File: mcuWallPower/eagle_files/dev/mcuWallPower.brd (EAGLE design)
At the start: 30 x 30 mm, 3 parts, among them P1 CR2032

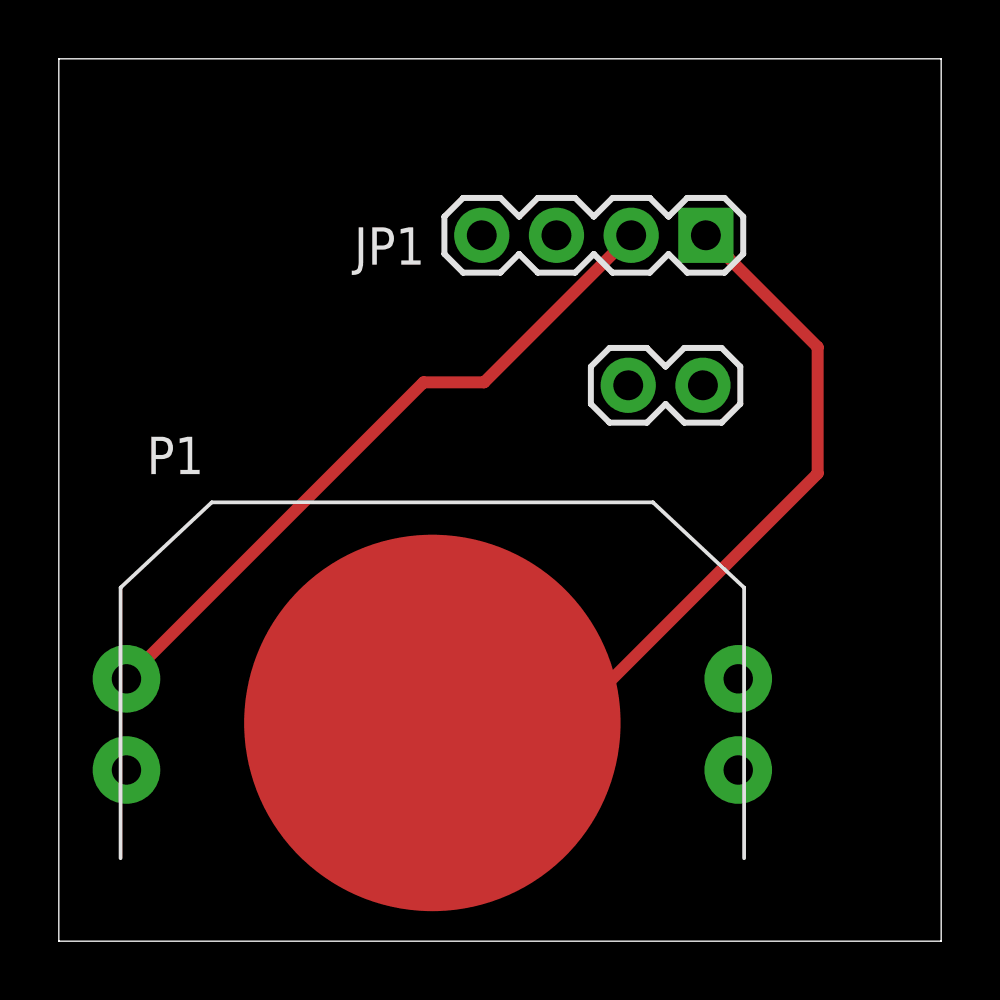
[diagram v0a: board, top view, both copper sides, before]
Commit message: Added USB mini connector to board along with other components. Todo: Replace USB mini connector with USB micro B connector. Looks like I'll need to make a custom footprint.
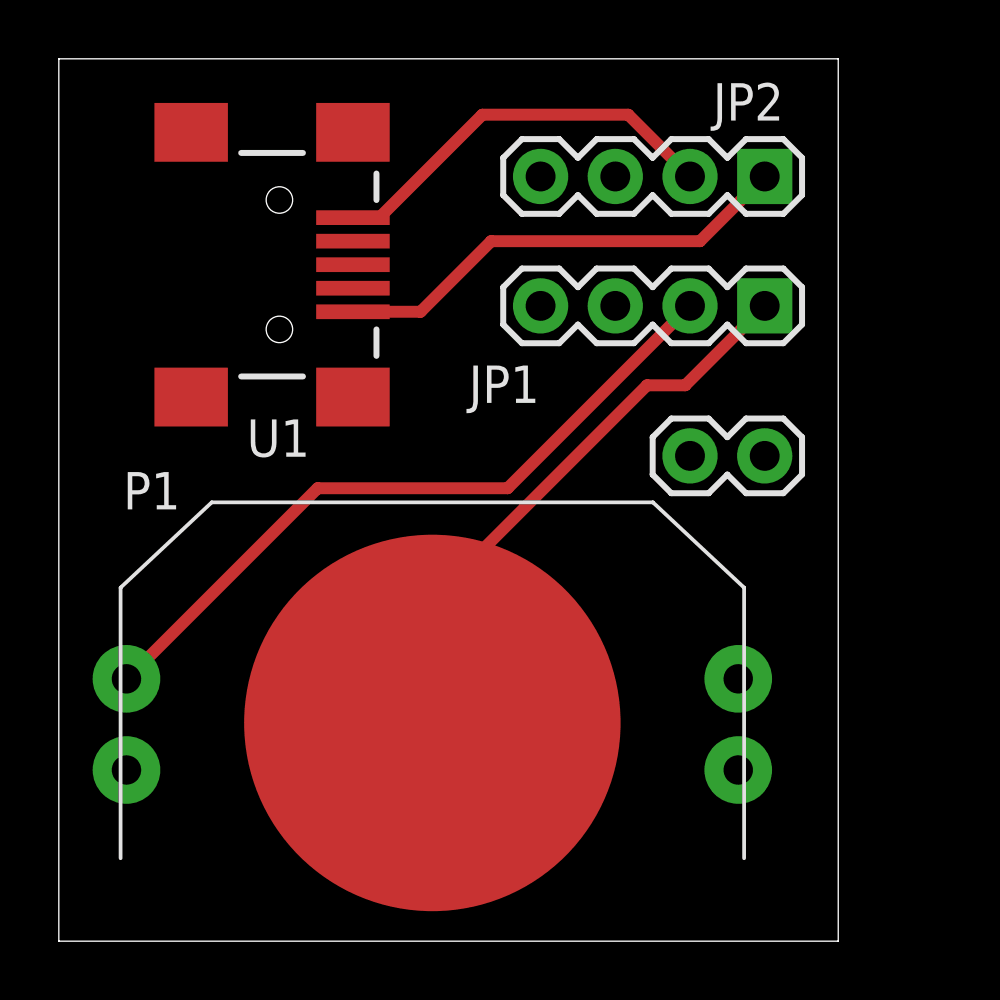
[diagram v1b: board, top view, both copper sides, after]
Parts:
- added JP2: (no value), SparkFun-Connectors:1X04
- added U1: USB-MINIB-5PIN, SparkFun-Connectors:USB-MINIB
- moved JP3 3.19 mm to (24.0, 16.5)
- moved JP1 3.12 mm to (24.0, 21.6)
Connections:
- new net N$3: JP2.1, U1.GND
- new net N$4: JP2.2, U1.VBUS
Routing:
- net N$3: track 0.00 -> 15.9 mm
- net N$4: track 0.00 -> 13.8 mm
- net N$2: track 26.3 -> 19.6 mm
- net N$1: track 23.4 -> 24.4 mm
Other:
- board size 30 x 30 mm -> 26.5 x 30 mm
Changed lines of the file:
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@@
 <board>
 <plain>
-<wire x1="0" y1="0" x2="30" y2="0" width="0" layer="20"/>
-<wire x1="30" y1="0" x2="30" y2="30" width="0" layer="20"/>
-<wire x1="30" y1="30" x2="0" y2="30" width="0" layer="20"/>
+<wire x1="0" y1="0" x2="26.5" y2="0" width="0" layer="20"/>
+<wire x1="26.5" y1="0" x2="26.5" y2="30" width="0" layer="20"/>
+<wire x1="26.5" y1="30" x2="0" y2="30" width="0" layer="20"/>
 <wire x1="0" y1="30" x2="0" y2="0" width="0" layer="20"/>
 </plain>
@@
 <elements>
 <element name="P1" library="freddyLibr" package="CR2032/2025" value="CR2032" x="12.7" y="7.42" smashed="yes">
-<attribute name="NAME" x="2.99" y="15.88" size="1.27" layer="25"/>
-</element>
-<element name="JP1" library="SparkFun-Connectors" package="1X04" value="" x="22" y="24" smashed="yes" rot="R180">
-<attribute name="NAME" x="12.4462" y="24.2712" size="1.27" layer="25" ratio="10" rot="R180"/>
-<attribute name="VALUE" x="23.27" y="27.175" size="1.27" layer="27" rot="R180"/>
-</element>
-<element name="JP3" library="SparkFun-Connectors" package="1X02" value="M02PTH" x="21.9" y="18.9" smashed="yes" rot="R180"/>
+<attribute name="NAME" x="2.19" y="14.68" size="1.27" layer="25"/>
+</element>
+<element name="JP1" library="SparkFun-Connectors" package="1X04" value="" x="24" y="21.6" smashed="yes" rot="R180">
+<attribute name="NAME" x="16.3462" y="19.5712" size="1.27" layer="25" ratio="10" rot="R180"/>
+<attribute name="VALUE" x="25.27" y="24.775" size="1.27" layer="27" rot="R180"/>
+</element>
+<element name="JP3" library="SparkFun-Connectors" package="1X02" value="M02PTH" x="24" y="16.5" smashed="yes" rot="R180"/>
+<element name="U1" library="SparkFun-Connectors" package="USB-MINIB" value="USB-MINIB-5PIN" x="7.5" y="23" smashed="yes">
+<attribute name="NAME" x="6.39" y="16.47" size="1.27" layer="25"/>
+</element>
+<element name="JP2" library="SparkFun-Connectors" package="1X04" value="" x="24" y="26" smashed="yes" rot="R180">
+<attribute name="NAME" x="24.6462" y="29.1712" size="1.27" layer="25" ratio="10" rot="R180"/>
+<attribute name="VALUE" x="25.27" y="29.175" size="1.27" layer="27" rot="R180"/>
+</element>
 </elements>
 <signals>
@@
 <contactref element="JP1" pad="2"/>
 <wire x1="2.3" y1="8.92" x2="2.32" y2="8.92" width="0.4064" layer="1"/>
-<wire x1="2.32" y1="8.92" x2="12.4" y2="19" width="0.4064" layer="1"/>
-<wire x1="12.4" y1="19" x2="14.46" y2="19" width="0.4064" layer="1"/>
-<wire x1="14.46" y1="19" x2="19.46" y2="24" width="0.4064" layer="1"/>
+<wire x1="2.32" y1="8.92" x2="8.8" y2="15.4" width="0.4064" layer="1"/>
+<wire x1="8.8" y1="15.4" x2="15.26" y2="15.4" width="0.4064" layer="1"/>
+<wire x1="15.26" y1="15.4" x2="21.46" y2="21.6" width="0.4064" layer="1"/>
 </signal>
 <signal name="N$2">
 <contactref element="P1" pad="GND"/>
 <contactref element="JP1" pad="1"/>
-<wire x1="12.7" y1="7.42" x2="17.32" y2="7.42" width="0.4064" layer="1"/>
-<wire x1="17.32" y1="7.42" x2="25.8" y2="15.9" width="0.4064" layer="1"/>
-<wire x1="25.8" y1="15.9" x2="25.8" y2="20.2" width="0.4064" layer="1"/>
-<wire x1="25.8" y1="20.2" x2="22" y2="24" width="0.4064" layer="1"/>
+<wire x1="12.7" y1="7.42" x2="12.7" y2="11.6" width="0.4064" layer="1"/>
+<wire x1="12.7" y1="11.6" x2="20" y2="18.9" width="0.4064" layer="1"/>
+<wire x1="20" y1="18.9" x2="21.3" y2="18.9" width="0.4064" layer="1"/>
+<wire x1="21.3" y1="18.9" x2="24" y2="21.6" width="0.4064" layer="1"/>
+</signal>
+<signal name="N$3">
+<contactref element="U1" pad="GND"/>
+<contactref element="JP2" pad="1"/>
+<wire x1="10" y1="21.4" x2="12.3" y2="21.4" width="0.4064" layer="1"/>
+<wire x1="12.3" y1="21.4" x2="14.7" y2="23.8" width="0.4064" layer="1"/>
+<wire x1="14.7" y1="23.8" x2="21.8" y2="23.8" width="0.4064" layer="1"/>
+<wire x1="21.8" y1="23.8" x2="24" y2="26" width="0.4064" layer="1"/>
+</signal>
+<signal name="N$4">
+<contactref element="U1" pad="VBUS"/>
+<contactref element="JP2" pad="2"/>
+<wire x1="10" y1="24.6" x2="10.9" y2="24.6" width="0.4064" layer="1"/>
+<wire x1="10.9" y1="24.6" x2="14.4" y2="28.1" width="0.4064" layer="1"/>
+<wire x1="14.4" y1="28.1" x2="19.36" y2="28.1" width="0.4064" layer="1"/>
+<wire x1="19.36" y1="28.1" x2="21.46" y2="26" width="0.4064" layer="1"/>
 </signal>
 </signals>

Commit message: mcuWallPower schematic and board updated. Ready for fitting.
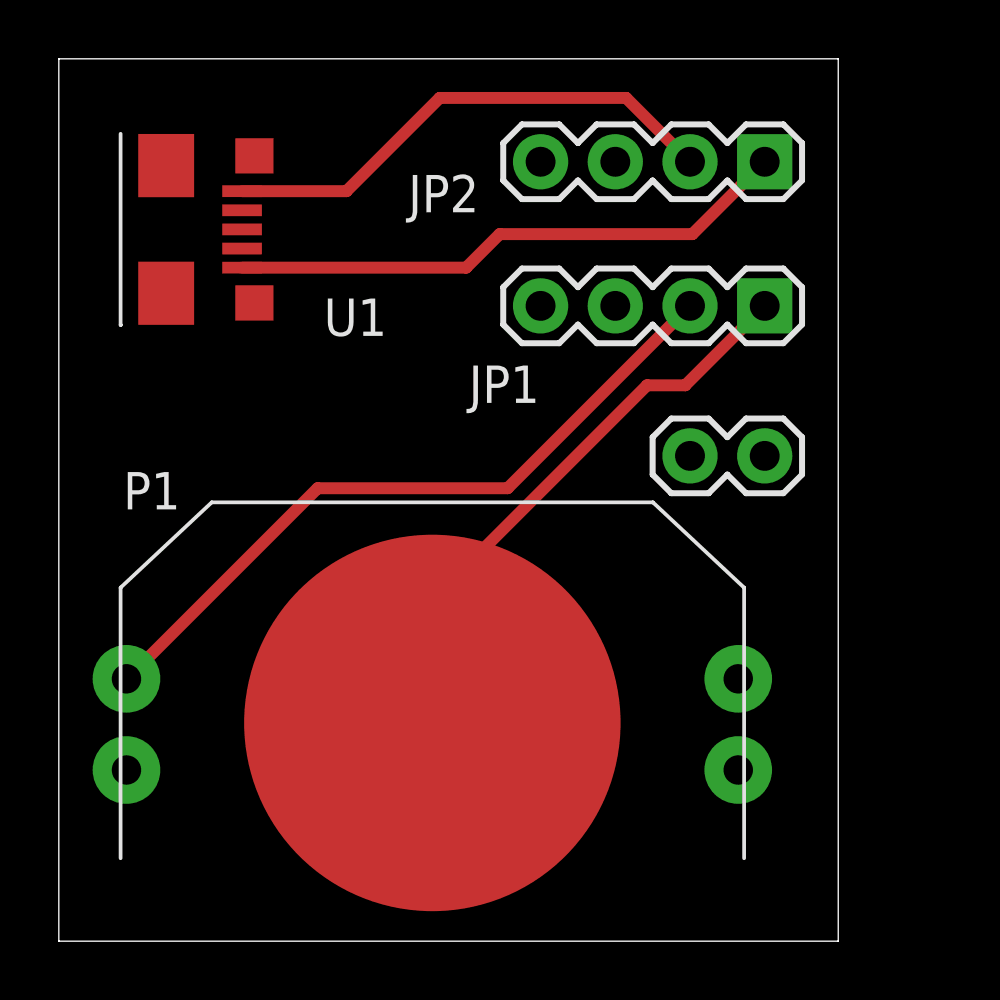
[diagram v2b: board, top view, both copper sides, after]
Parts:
- U1: value USB-MINIB-5PIN -> USB-MICROB-SMT5-PIN; device SparkFun-Connectors:USB-MINIB -> freddyLibr:USB-MICROB-SMT
- moved U1 3.14 mm to (4.60, 24.2), turned to 270 degrees
- moved JP2 0.50 mm to (24.0, 26.5)
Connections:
- net N$3: now also U1.9; no longer U1.GND
- net N$4: now also U1.5; no longer U1.VBUS
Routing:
- net N$4: track 13.8 -> 17.4 mm
- net N$3: track 15.9 -> 19.3 mm
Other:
- board text added: "F. Lee 12/25/2013 mcuWallPower"
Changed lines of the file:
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@@
 <setting verticaltext="up"/>
 </settings>
-<grid distance="0.1" unitdist="mm" unit="mm" style="lines" multiple="1" display="yes" altdistance="0.025" altunitdist="inch" altunit="mm"/>
+<grid distance="0.01" unitdist="mm" unit="mm" style="lines" multiple="1" display="yes" altdistance="0.025" altunitdist="inch" altunit="mm"/>
 <layers>
 <layer number="1" name="Top" color="4" fill="1" visible="yes" active="yes"/>
@@
 <wire x1="26.5" y1="30" x2="0" y2="30" width="0" layer="20"/>
 <wire x1="0" y1="30" x2="0" y2="0" width="0" layer="20"/>
+<text x="1.98" y="16.96" size="0.75" layer="51">F. Lee
+12/25/2013
+mcuWallPower</text>
 </plain>
 <attributes>
@@
 </element>
 <element name="JP3" library="SparkFun-Connectors" package="1X02" value="M02PTH" x="24" y="16.5" smashed="yes" rot="R180"/>
-<element name="U1" library="SparkFun-Connectors" package="USB-MINIB" value="USB-MINIB-5PIN" x="7.5" y="23" smashed="yes">
-<attribute name="NAME" x="6.39" y="16.47" size="1.27" layer="25"/>
+<element name="JP2" library="SparkFun-Connectors" package="1X04" value="" x="24" y="26.5" smashed="yes" rot="R180">
+<attribute name="NAME" x="14.2862" y="26.0512" size="1.27" layer="25" ratio="10" rot="R180"/>
+<attribute name="VALUE" x="25.27" y="29.675" size="1.27" layer="27" rot="R180"/>
 </element>
-<element name="JP2" library="SparkFun-Connectors" package="1X04" value="" x="24" y="26" smashed="yes" rot="R180">
-<attribute name="NAME" x="24.6462" y="29.1712" size="1.27" layer="25" ratio="10" rot="R180"/>
-<attribute name="VALUE" x="25.27" y="29.175" size="1.27" layer="27" rot="R180"/>
+<element name="U1" library="freddyLibr" package="USB-MICROB-SMT" value="USB-MICROB-SMT5-PIN" x="4.6" y="24.2" smashed="yes" rot="R270">
+<attribute name="NAME" x="9.01" y="20.58" size="1.27" layer="25"/>
 </element>
 </elements>
@@
 </signal>
 <signal name="N$3">
-<contactref element="U1" pad="GND"/>
 <contactref element="JP2" pad="1"/>
-<wire x1="10" y1="21.4" x2="12.3" y2="21.4" width="0.4064" layer="1"/>
-<wire x1="12.3" y1="21.4" x2="14.7" y2="23.8" width="0.4064" layer="1"/>
-<wire x1="14.7" y1="23.8" x2="21.8" y2="23.8" width="0.4064" layer="1"/>
-<wire x1="21.8" y1="23.8" x2="24" y2="26" width="0.4064" layer="1"/>
+<contactref element="U1" pad="9"/>
+<wire x1="6.23" y1="22.9" x2="13.85" y2="22.9" width="0.4064" layer="1"/>
+<wire x1="13.85" y1="22.9" x2="14.99" y2="24.04" width="0.4064" layer="1"/>
+<wire x1="14.99" y1="24.04" x2="21.54" y2="24.04" width="0.4064" layer="1"/>
+<wire x1="21.54" y1="24.04" x2="24" y2="26.5" width="0.4064" layer="1"/>
 </signal>
 <signal name="N$4">
-<contactref element="U1" pad="VBUS"/>
+<contactref element="U1" pad="5"/>
 <contactref element="JP2" pad="2"/>
-<wire x1="10" y1="24.6" x2="10.9" y2="24.6" width="0.4064" layer="1"/>
-<wire x1="10.9" y1="24.6" x2="14.4" y2="28.1" width="0.4064" layer="1"/>
-<wire x1="14.4" y1="28.1" x2="19.36" y2="28.1" width="0.4064" layer="1"/>
-<wire x1="19.36" y1="28.1" x2="21.46" y2="26" width="0.4064" layer="1"/>
+<wire x1="6.23" y1="25.5" x2="9.78" y2="25.5" width="0.4064" layer="1"/>
+<wire x1="9.78" y1="25.5" x2="12.95" y2="28.67" width="0.4064" layer="1"/>
+<wire x1="12.95" y1="28.67" x2="19.29" y2="28.67" width="0.4064" layer="1"/>
+<wire x1="19.29" y1="28.67" x2="21.46" y2="26.5" width="0.4064" layer="1"/>
 </signal>
 </signals>
 </board>
 </drawing>
+<compatibility>
+<note version="6.3" minversion="6.2.2" severity="warning">
+Since Version 6.2.2 text objects can contain more than one line,
+which will not be processed correctly with this version.
+</note>
+</compatibility>
 </eagle>

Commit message: latest project files. using latest footprint for USB-micro-B component.
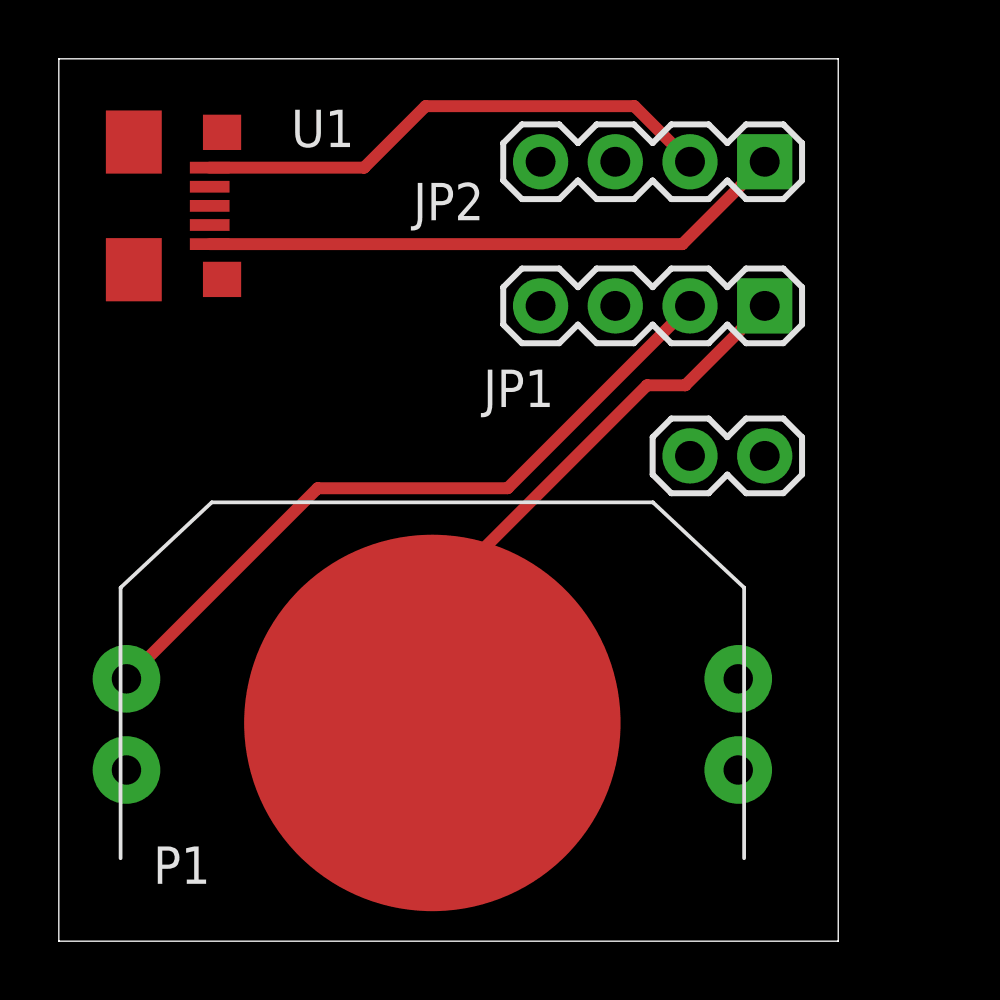
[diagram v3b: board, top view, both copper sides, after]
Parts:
- moved U1 1.36 mm to (3.50, 25.0)
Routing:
- net N$3: track 19.3 -> 20.0 mm
- net N$4: track 17.4 -> 18.0 mm
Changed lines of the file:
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@@
 <wire x1="26.5" y1="30" x2="0" y2="30" width="0" layer="20"/>
 <wire x1="0" y1="30" x2="0" y2="0" width="0" layer="20"/>
-<text x="1.98" y="16.96" size="0.75" layer="51">F. Lee
+<text x="2.81" y="16.77" size="1" layer="51">F. Lee
 12/25/2013
 mcuWallPower</text>
@@
 <elements>
 <element name="P1" library="freddyLibr" package="CR2032/2025" value="CR2032" x="12.7" y="7.42" smashed="yes">
-<attribute name="NAME" x="2.19" y="14.68" size="1.27" layer="25"/>
+<attribute name="NAME" x="3.21" y="1.95" size="1.27" layer="25"/>
 </element>
 <element name="JP1" library="SparkFun-Connectors" package="1X04" value="" x="24" y="21.6" smashed="yes" rot="R180">
-<attribute name="NAME" x="16.3462" y="19.5712" size="1.27" layer="25" ratio="10" rot="R180"/>
+<attribute name="NAME" x="16.8362" y="19.4312" size="1.27" layer="25" ratio="10" rot="R180"/>
 <attribute name="VALUE" x="25.27" y="24.775" size="1.27" layer="27" rot="R180"/>
 </element>
 <element name="JP3" library="SparkFun-Connectors" package="1X02" value="M02PTH" x="24" y="16.5" smashed="yes" rot="R180"/>
 <element name="JP2" library="SparkFun-Connectors" package="1X04" value="" x="24" y="26.5" smashed="yes" rot="R180">
-<attribute name="NAME" x="14.2862" y="26.0512" size="1.27" layer="25" ratio="10" rot="R180"/>
+<attribute name="NAME" x="14.4562" y="25.7812" size="1.27" layer="25" ratio="10" rot="R180"/>
 <attribute name="VALUE" x="25.27" y="29.675" size="1.27" layer="27" rot="R180"/>
 </element>
-<element name="U1" library="freddyLibr" package="USB-MICROB-SMT" value="USB-MICROB-SMT5-PIN" x="4.6" y="24.2" smashed="yes" rot="R270">
-<attribute name="NAME" x="9.01" y="20.58" size="1.27" layer="25"/>
+<element name="U1" library="freddyLibr" package="USB-MICROB-SMT" value="USB-MICROB-SMT5-PIN" x="3.5" y="25" smashed="yes" rot="R270">
+<attribute name="NAME" x="7.9" y="27" size="1.27" layer="25"/>
 </element>
 </elements>
@@
 <contactref element="JP2" pad="1"/>
 <contactref element="U1" pad="9"/>
-<wire x1="6.23" y1="22.9" x2="13.85" y2="22.9" width="0.4064" layer="1"/>
-<wire x1="13.85" y1="22.9" x2="14.99" y2="24.04" width="0.4064" layer="1"/>
-<wire x1="14.99" y1="24.04" x2="21.54" y2="24.04" width="0.4064" layer="1"/>
-<wire x1="21.54" y1="24.04" x2="24" y2="26.5" width="0.4064" layer="1"/>
+<wire x1="5.13" y1="23.7" x2="21.2" y2="23.7" width="0.4064" layer="1"/>
+<wire x1="21.2" y1="23.7" x2="24" y2="26.5" width="0.4064" layer="1"/>
 </signal>
 <signal name="N$4">
+<contactref element="JP2" pad="2"/>
 <contactref element="U1" pad="5"/>
-<contactref element="JP2" pad="2"/>
-<wire x1="6.23" y1="25.5" x2="9.78" y2="25.5" width="0.4064" layer="1"/>
-<wire x1="9.78" y1="25.5" x2="12.95" y2="28.67" width="0.4064" layer="1"/>
-<wire x1="12.95" y1="28.67" x2="19.29" y2="28.67" width="0.4064" layer="1"/>
-<wire x1="19.29" y1="28.67" x2="21.46" y2="26.5" width="0.4064" layer="1"/>
+<wire x1="5.13" y1="26.3" x2="10.38" y2="26.3" width="0.4064" layer="1"/>
+<wire x1="10.38" y1="26.3" x2="12.47" y2="28.39" width="0.4064" layer="1"/>
+<wire x1="12.47" y1="28.39" x2="19.57" y2="28.39" width="0.4064" layer="1"/>
+<wire x1="19.57" y1="28.39" x2="21.46" y2="26.5" width="0.4064" layer="1"/>
 </signal>
 </signals>
